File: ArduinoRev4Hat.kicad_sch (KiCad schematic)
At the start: 5 parts, among them J1 Conn_01x10_Pin, J2 Conn_01x08_Pin, J3 Conn_01x04_Pin, J4 Conn_01x04_Pin, J5 Conn_01x04_Pin

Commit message: First attempted at wiring; waiting for Tyler's Review
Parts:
- added J10, J11, J6, J7, J8, J9: 73099-0, 73099-0:POMONA_73099-0, symbol 73099-0:73099-0
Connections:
- net GND: now also J6.1, J7.1, J8.1
- net VM: now reaches J4.2 (Pin_2)
- net VM: now also J3.2 (Pin_2), J5.2 (Pin_2), J10.1, J11.1, J9.1
- no-connect marks 0 -> 9
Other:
- note added: "Power Supply Each need a GND"

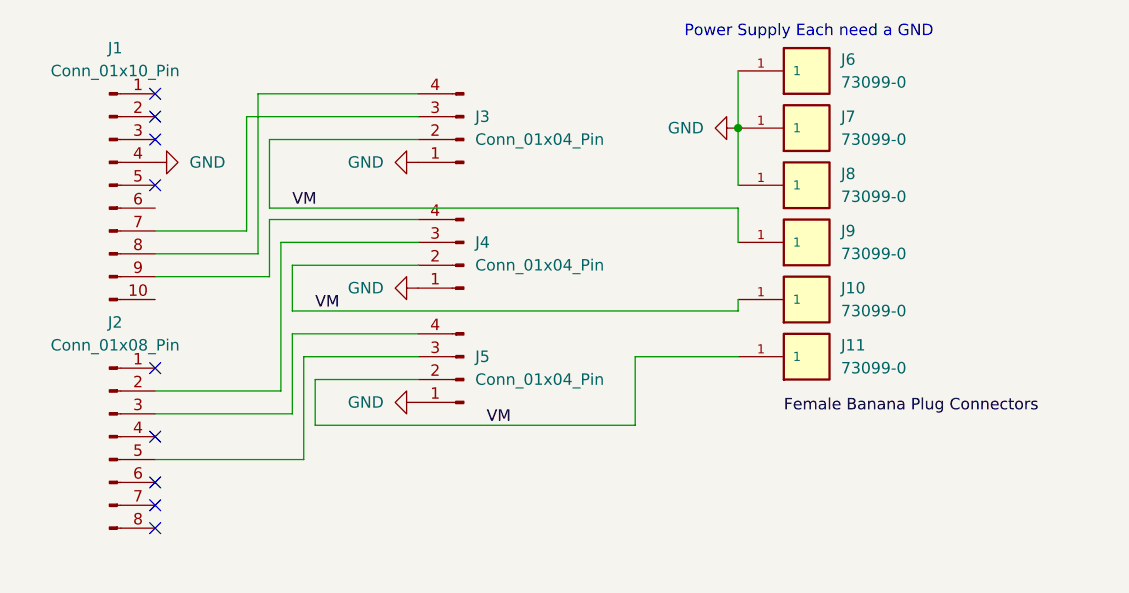
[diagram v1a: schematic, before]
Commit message: Layed out the board. Still awaiting review
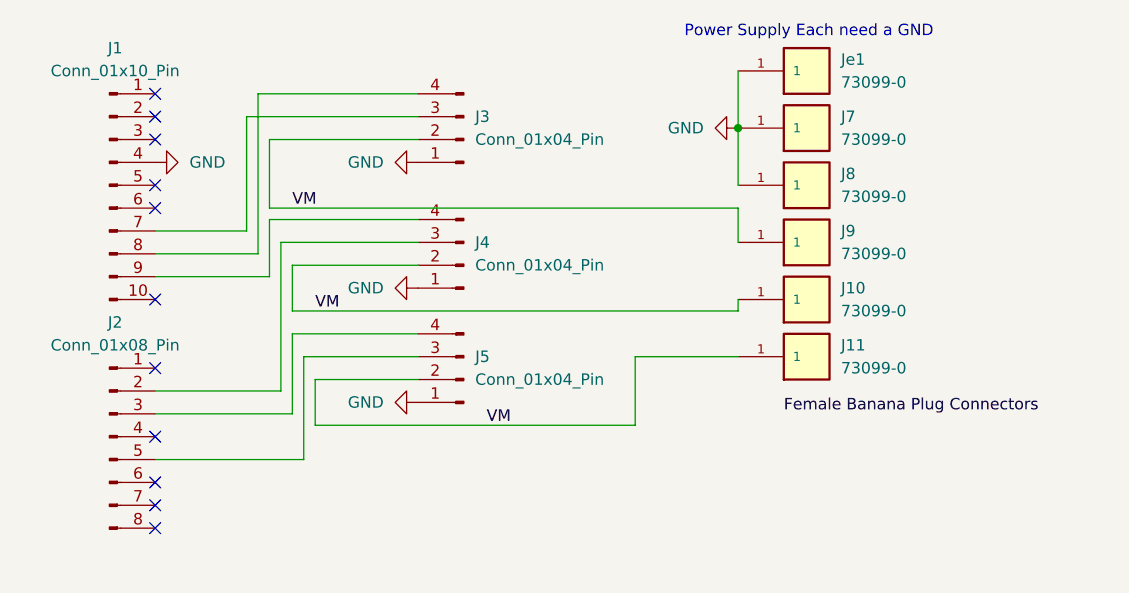
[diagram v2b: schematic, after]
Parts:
- J10, J11, J7, J8, J9: footprint 73099-0:POMONA_73099-0 -> my_custom:POMONA_73099-0
- J3, J4, J5: footprint (none) -> Connector_PinHeader_2.54mm:PinHeader_1x04_P2.54mm_Vertical
- Je1: renamed from J6; footprint 73099-0:POMONA_73099-0 -> my_custom:POMONA_73099-0
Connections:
- no-connect marks 9 -> 11
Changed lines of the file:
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@@
+	)
+	(no_connect
+		(at 72.39 64.77)
 	)
 	(no_connect
@@
 	(no_connect
 		(at 72.39 72.39)
+	)
+	(no_connect
+		(at 72.39 54.61)
 	)
 	(no_connect
@@
 			)
 		)
-		(property "Footprint" "73099-0:POMONA_73099-0"
+		(property "Footprint" "my_custom:POMONA_73099-0"
 			(at 144.78 71.12 0)
 			(effects
@@
 		(dnp no)
 		(fields_autoplaced yes)
-		(property "Reference" "J6"
+		(property "Reference" "Je1"
 			(at 148.59 38.0999 0)
 			(effects
@@
 			)
 		)
-		(property "Footprint" "73099-0:POMONA_73099-0"
+		(property "Footprint" "my_custom:POMONA_73099-0"
 			(at 144.78 39.37 0)
 			(effects
@@
 			(project ""
 				(path "/3cd5f95e-5b22-4342-86a1-cdbd217d3c5d"
-					(reference "J6")
+					(reference "Je1")
 					(unit 1)
 				)
@@
 			)
 		)
-		(property "Footprint" "73099-0:POMONA_73099-0"
+		(property "Footprint" "my_custom:POMONA_73099-0"
 			(at 144.78 64.77 0)
 			(effects
@@
 			)
 		)
-		(property "Footprint" ""
+		(property "Footprint" "Connector_PinHeader_2.54mm:PinHeader_1x04_P2.54mm_Vertical"
 			(at 106.68 60.96 0)
 			(effects
@@
 			)
 		)
-		(property "Footprint" "73099-0:POMONA_73099-0"
+		(property "Footprint" "my_custom:POMONA_73099-0"
 			(at 144.78 52.07 0)
 			(effects
@@
 			)
 		)
-		(property "Footprint" "73099-0:POMONA_73099-0"
+		(property "Footprint" "my_custom:POMONA_73099-0"
 			(at 144.78 58.42 0)
 			(effects
@@
 			)
 		)
-		(property "Footprint" "73099-0:POMONA_73099-0"
+		(property "Footprint" "my_custom:POMONA_73099-0"
 			(at 144.78 45.72 0)
 			(effects
@@
 			)
 		)
-		(property "Footprint" ""
+		(property "Footprint" "Connector_PinHeader_2.54mm:PinHeader_1x04_P2.54mm_Vertical"
 			(at 106.68 46.99 0)
 			(effects
@@
 			)
 		)
-		(property "Footprint" ""
+		(property "Footprint" "Connector_PinHeader_2.54mm:PinHeader_1x04_P2.54mm_Vertical"
 			(at 106.68 73.66 0)
 			(effects

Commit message: uploading diagram
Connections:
- net IN1_Y: now reaches J2.2 (Pin_2), J4.3 (Pin_3)
- net IN2_Z: now reaches J2.3 (Pin_3), J5.4 (Pin_4)
- net IN1_Z: now reaches J2.5 (Pin_5), J5.3 (Pin_3)
- net IN2_Y: now reaches J1.9 (Pin_9), J4.4 (Pin_4)
- net IN1_X: now reaches J1.7 (Pin_7), J3.3 (Pin_3)
- net IN2_X: now reaches J1.8 (Pin_8), J3.4 (Pin_4)
- removed net VM: J10.1, J11.1, J3.2 (Pin_2), J4.2 (Pin_2), J5.2 (Pin_2), J9.1
- new net VM_X: J3.2 (Pin_2), J9.1
- new net VM_Y: J10.1, J4.2 (Pin_2)
- new net VM_Z: J11.1, J5.2 (Pin_2)
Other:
- note added: "Arduino Pins"
- note added: "Banana Plugs"
- note added: "H-Bridges"
- note removed: "Power Supply Each need a GND"
- moved on the sheet: J10, J11, J3, J4, J5, J7, J8, J9, Je1

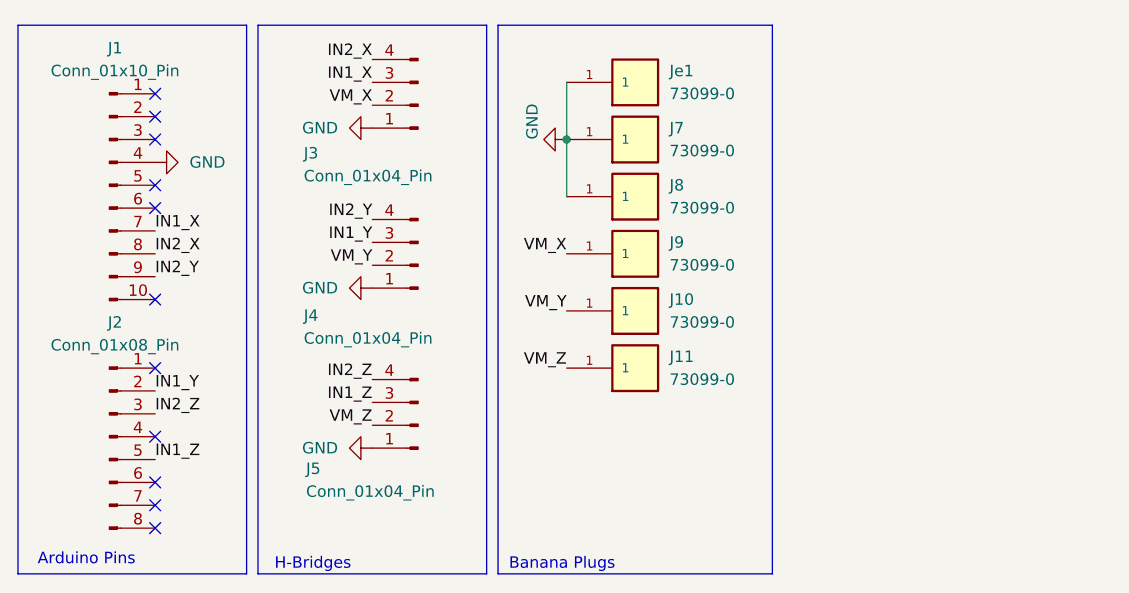
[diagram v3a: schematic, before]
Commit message: changed logo; moved banana plugs location; swaped in1_x and in2_x pin for a better layout;
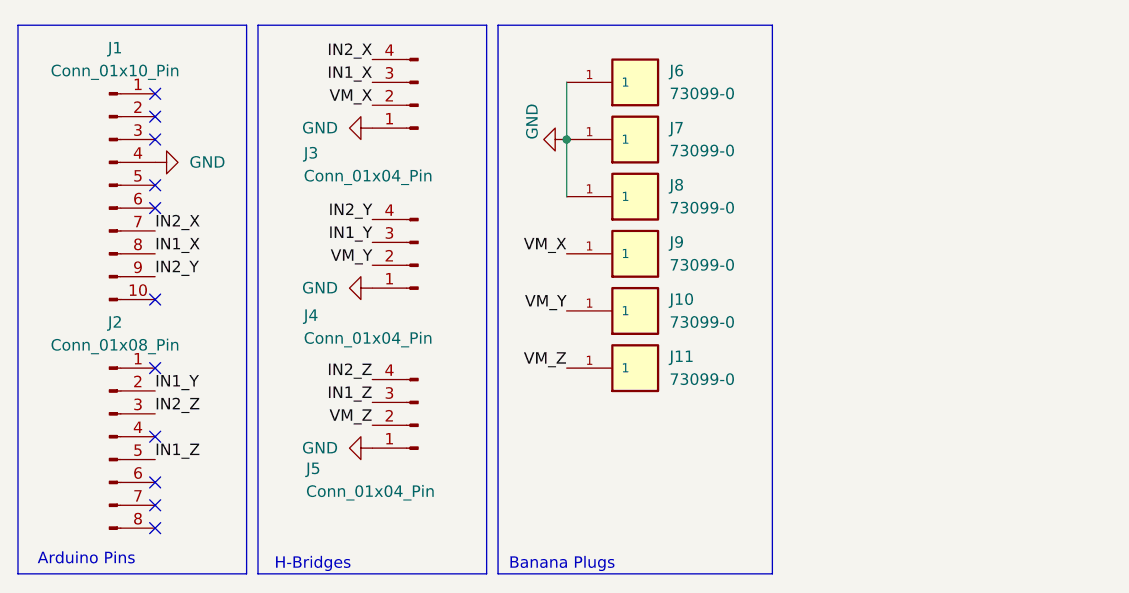
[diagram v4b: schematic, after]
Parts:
- renumbered Je1 to J6
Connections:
- net IN1_X: now also J1.8 (Pin_8); no longer J1.7 (Pin_7)
- net IN2_X: now also J1.7 (Pin_7); no longer J1.8 (Pin_8)
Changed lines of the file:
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@@
 		)
 	)
-	(label "IN2_X"
+	(label "IN1_X"
 		(at 72.39 59.69 0)
+		(fields_autoplaced yes)
 		(effects
 			(font
@@
 	(label "VM_X"
 		(at 118.11 59.69 180)
-		(effects
-			(font
-				(size 1.27 1.27)
-			)
-			(justify right bottom)
-		)
-	)
-	(label "IN1_X"
+		(fields_autoplaced yes)
+		(effects
+			(font
+				(size 1.27 1.27)
+			)
+			(justify right bottom)
+		)
+	)
+	(label "IN2_X"
 		(at 72.39 57.15 0)
+		(fields_autoplaced yes)
 		(effects
 			(font
@@
 	(label "VM_Z"
 		(at 96.52 78.74 180)
+		(fields_autoplaced yes)
 		(effects
 			(font
@@
 	(label "IN1_Z"
 		(at 96.52 76.2 180)
+		(fields_autoplaced yes)
 		(effects
 			(font
@@
 	(label "VM_Z"
 		(at 118.11 72.39 180)
+		(fields_autoplaced yes)
 		(effects
 			(font
@@
 	(label "IN2_Z"
 		(at 72.39 77.47 0)
+		(fields_autoplaced yes)
 		(effects
 			(font
@@
 	(label "IN2_Y"
 		(at 72.39 62.23 0)
+		(fields_autoplaced yes)
 		(effects
 			(font
@@
 	(label "VM_X"
 		(at 96.52 43.18 180)
+		(fields_autoplaced yes)
 		(effects
 			(font
@@
 	(label "IN2_Z"
 		(at 96.52 73.66 180)
+		(fields_autoplaced yes)
 		(effects
 			(font
@@
 	(label "IN1_Y"
 		(at 96.52 58.42 180)
+		(fields_autoplaced yes)
 		(effects
 			(font
@@
 	(label "VM_Y"
 		(at 118.11 66.04 180)
+		(fields_autoplaced yes)
 		(effects
 			(font
@@
 	(label "IN2_Y"
 		(at 96.52 55.88 180)
+		(fields_autoplaced yes)
 		(effects
 			(font
@@
 	(label "IN1_Z"
 		(at 72.39 82.55 0)
+		(fields_autoplaced yes)
 		(effects
 			(font
@@
 	(label "IN1_Y"
 		(at 72.39 74.93 0)
+		(fields_autoplaced yes)
 		(effects
 			(font
@@
 	(label "VM_Y"
 		(at 96.52 60.96 180)
+		(fields_autoplaced yes)
 		(effects
 			(font
@@
 		(dnp no)
 		(fields_autoplaced yes)
-		(property "Reference" "Je1"
+		(property "Reference" "J6"
 			(at 129.54 39.3699 0)
 			(effects
@@
 			(project ""
 				(path "/3cd5f95e-5b22-4342-86a1-cdbd217d3c5d"
-					(reference "Je1")
+					(reference "J6")
 					(unit 1)
 				)
